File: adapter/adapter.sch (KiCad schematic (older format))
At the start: 0 parts

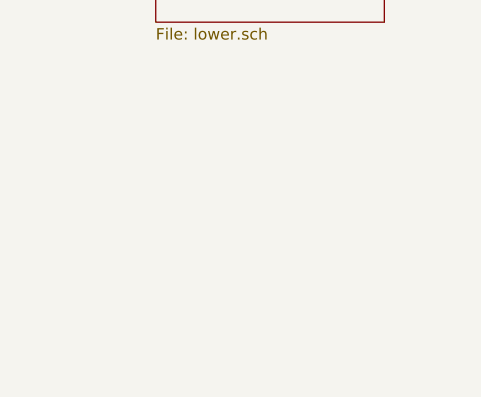
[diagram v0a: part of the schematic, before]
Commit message: Add mouse bites
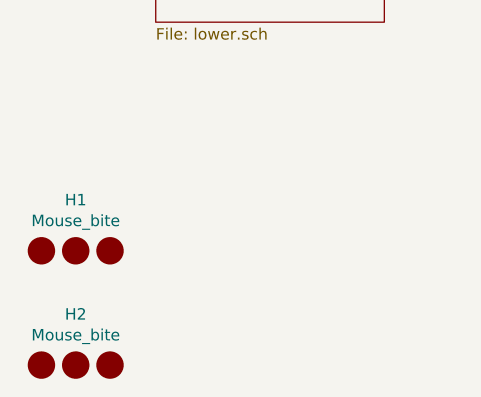
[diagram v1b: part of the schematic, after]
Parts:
- added H1, H2: Mouse_bite, node:single_sided_tab_5mm, symbol node:Mouse_bite
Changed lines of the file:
@@
 F1 "upper.sch" 50
 $EndSheet
+$Comp
+L node:Mouse_bite H1
+U 1 1 5FBB7FE6
+P 4150 5000
+F 0 "H1" H 4150 5222 50  0000 C CNN
+F 1 "Mouse_bite" H 4150 5131 50  0000 C CNN
+F 2 "node:single_sided_tab_5mm" H 4150 5000 50  0001 C CNN
+F 3 "" H 4150 5000 50  0001 C CNN
+	1    4150 5000
+	1    0    0    -1
+$EndComp
+$Comp
+L node:Mouse_bite H2
+U 1 1 5FBB81D7
+P 4150 5500
+F 0 "H2" H 4150 5722 50  0000 C CNN
+F 1 "Mouse_bite" H 4150 5631 50  0000 C CNN
+F 2 "node:single_sided_tab_5mm" H 4150 5500 50  0001 C CNN
+F 3 "" H 4150 5500 50  0001 C CNN
+	1    4150 5500
+	1    0    0    -1
+$EndComp
 $EndSCHEMATC
